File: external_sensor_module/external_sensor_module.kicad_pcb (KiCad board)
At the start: 2 copper layers, 159.4 x 56.8 mm, 51 parts, among them J1 platform UART, J2 USB_C_Sensors, J3 CSI2 Camera, J4 Lidar, J5 MSD-4-A, J6 Power, J7 Conn_01x04, J8 Conn_01x11, J9 USB_C_Radar, SW1 RST, U1 MLX90614ESF-BAA-000-TU, U2 USBLC6-2SC6, U3 BNO085, U4 USBLC6-2SC6, U5 ESP32-P4_MODULE

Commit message: update 261016
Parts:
- moved D4 78.4 mm to (231.2, 127.8), turned to 180 degrees
- moved SW1 75.3 mm to (225.1, 88.2), turned to 90 degrees
- moved C5 70.4 mm to (230.7, 122.3), turned to 0 degrees
- moved J6 70.2 mm to (225.5, 132.4), turned to 0 degrees
- moved C4 69.3 mm to (231.4, 113.0), turned to 90 degrees
- moved D2 66.6 mm to (223.5, 127.8), turned to 0 degrees
- moved R7 66.4 mm to (227.0, 97.6), turned to -90 degrees
- moved PS1 65.3 mm to (229.4, 119.1), turned to 90 degrees
- moved L1 63.8 mm to (228.9, 115.0), turned to 90 degrees
- moved C7 62.5 mm to (226.1, 100.4), turned to 0 degrees
- moved R11 62.4 mm to (228.1, 111.8), turned to 0 degrees
- moved C6 60.9 mm to (226.1, 102.7), turned to 0 degrees
- moved R10 59.3 mm to (226.7, 115.0), turned to 90 degrees
- moved C1 51.2 mm to (180.2, 109.5), turned to 90 degrees
- moved J4 49.2 mm to (205.0, 132.5), turned to 0 degrees
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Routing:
- net +3V3: track 109.8 -> 31.8 mm, vias 3 -> 1
- net +5V: track 60.5 -> 2.81 mm
- net /external_sensor_module/usb-: track 23.0 -> 0.00 mm
- net /external_sensor_module/usb+: track 23.0 -> 0.00 mm
- net /external_sensor_module/LTX: track 22.7 -> 0.00 mm
- net /external_sensor_module/LRX: track 21.3 -> 0.00 mm
- net /external_sensor_module/SD_VDD: track 13.3 -> 0.00 mm
- net Net-(C1-Pad1): track 29.0 -> 16.0 mm
- net /external_sensor_module/CSI_D0-: track 19.0 -> 29.2 mm
- net /external_sensor_module/CSI_D0+: track 19.8 -> 28.4 mm
- net /external_sensor_module/CSI0: track 8.24 -> 15.3 mm, vias 0 -> 2
- net /external_sensor_module/CSI1: track 7.52 -> 13.9 mm, vias 0 -> 2
- net /external_sensor_module/I2C SCL: track 7.38 -> 12.6 mm, vias 0 -> 2
- net /external_sensor_module/CSI_CLK+: track 35.7 -> 30.6 mm
- net /external_sensor_module/I2C SDA: track 8.00 -> 12.0 mm, vias 0 -> 2
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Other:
- board size 159.4 x 56.8 mm -> 159.4 x 56.4 mm

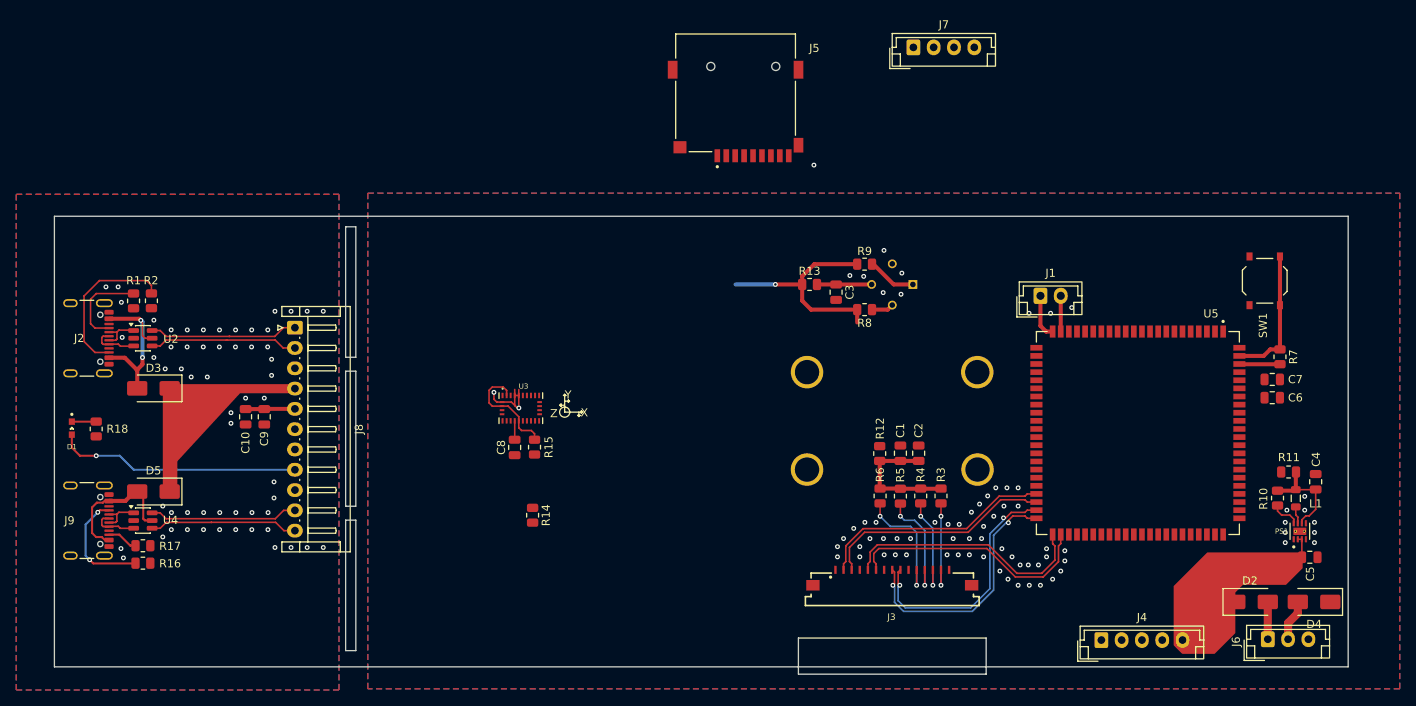
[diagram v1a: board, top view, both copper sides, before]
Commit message: updated layout
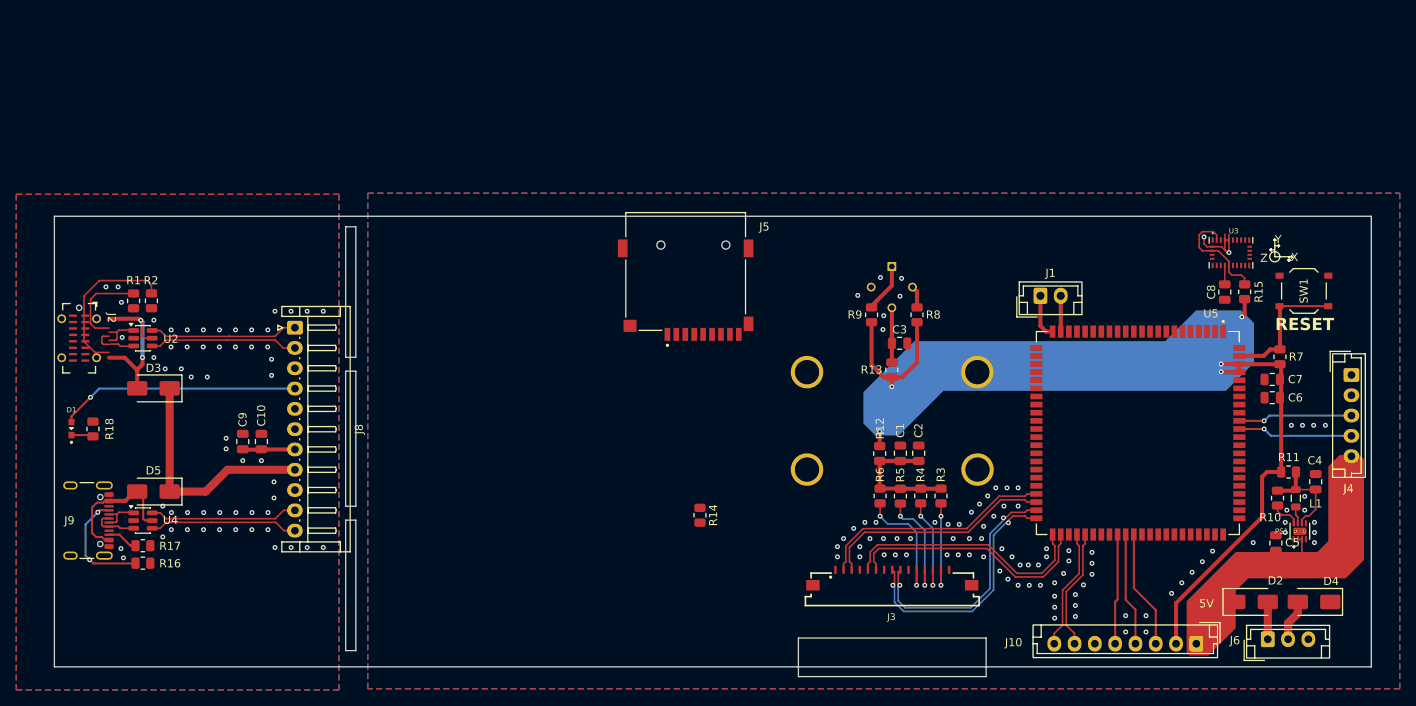
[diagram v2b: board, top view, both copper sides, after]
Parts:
- removed J7: Conn_01x04, Connector_JST:JST_EH_B4B-EH-A_1x04_P2.50mm_Vertical
- added J10: Conn_01x08, Connector_JST:JST_EH_B8B-EH-A_1x08_P2.50mm_Vertical, F.Cu at (216.7, 132.9)
- J2: footprint Connector_USB:USB_C_Receptacle_GCT_USB4105-xx-A_16P_TopMnt_Horizontal -> Connector_USB:USB_C_Receptacle_G-Switch_GT-USB-7051x
- moved R15 89.5 mm to (222.7, 89.6)
- moved U3 89.5 mm to (221.0, 84.8)
- moved C8 89.5 mm to (220.2, 89.6)
- moved J4 44.9 mm to (235.8, 99.8), turned to -90 degrees
- moved J5 22.8 mm to (153.8, 87.1)
- moved R14 20.6 mm to (155.6, 117.1)
- moved R13 14.6 mm to (179.2, 99.2), turned to 90 degrees
- moved C3 10.0 mm to (180.2, 96.0), turned to 0 degrees
- moved R8 6.49 mm to (182.3, 92.4), turned to -90 degrees
- moved R9 6.29 mm to (176.7, 92.4), turned to -90 degrees
- moved SW1 4.98 mm to (229.9, 89.5), turned to 0 degrees
- moved C5 4.53 mm to (226.5, 120.5), turned to 90 degrees
- moved C9 4.04 mm to (99.2, 108.0), turned to 90 degrees
- moved C10 3.62 mm to (101.5, 108.0), turned to 90 degrees
- moved R18 0.40 mm to (80.8, 106.5), turned to -90 degrees
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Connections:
- J8 pad 4: /IO plate/IO_5V -> /IO plate/IO_LED
- J8 pad 5: /IO plate/IO_3V3 -> /IO plate/IO_SDA
- J8 pad 6: /IO plate/IO_SDA -> /IO plate/IO_SCL
- J8 pad 7: /IO plate/IO_SCL -> /IO plate/IO_3V3
- J8 pad 8: /IO plate/IO_LED -> /IO plate/IO_5V
- U5 pad 53: unconnected-(U5-GPIO26-Pad53) -> /external_sensor_module/LED
- U5 pad 54: unconnected-(U5-GPIO27-Pad54) -> /external_sensor_module/SDA
- U5 pad 55: unconnected-(U5-GPIO28-Pad55) -> /external_sensor_module/SCL
- U5 pad 58: /external_sensor_module/LRX -> unconnected-(U5-GPIO31-Pad58)
- U5 pad 59: /external_sensor_module/LTX -> unconnected-(U5-GPIO32-Pad59)
- U5 pad 78: unconnected-(U5-GPIO50-Pad78) -> /external_sensor_module/LTX
- U5 pad 79: unconnected-(U5-GPIO51-Pad79) -> /external_sensor_module/LRX
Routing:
- net +3V3: track 31.8 -> 73.3 mm, vias 1 -> 5
- net /external_sensor_module/usb-: track 0.00 -> 14.8 mm
- net /external_sensor_module/usb+: track 0.00 -> 14.8 mm
- net /external_sensor_module/SCL: track 0.00 -> 14.6 mm
- net /external_sensor_module/LTX: track 0.00 -> 14.2 mm, vias 0 -> 1
- net /external_sensor_module/LRX: track 0.00 -> 14.1 mm, vias 0 -> 1
- net /external_sensor_module/SDA: track 0.00 -> 13.9 mm
- net /external_sensor_module/LED: track 0.00 -> 13.6 mm
- net /IO plate/IO_5V: track 28.1 -> 29.3 mm
- net /IO plate/IO_LED: track 30.2 -> 29.6 mm
- net GND: track 8.86 -> 9.02 mm, vias 129 -> 149
- net +5V: vias 1 -> 0
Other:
- board size 159.4 x 56.4 mm -> 162.2 x 56.7 mm
- board text added: "5V"
- board text added: "RESET"

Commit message: new pcb layout
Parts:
- added Q1: TSM500P02CX_RFG, Library:TRANS_TSM500P02CX_RFG, F.Cu at (147.8, 105.3)
- J2: footprint Connector_USB:USB_C_Receptacle_G-Switch_GT-USB-7051x -> Connector_USB:USB_C_Receptacle_GCT_USB4105-xx-A_16P_TopMnt_Horizontal
- moved R14 7.71 mm to (149.4, 112.5)
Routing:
- net Net-(C1-Pad1): track 16.0 -> 27.9 mm, vias 0 -> 2
- net GND: track 9.02 -> 13.7 mm, vias 149 -> 146
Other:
- board text added: "RADAR"
- board text added: "SENSOR"
